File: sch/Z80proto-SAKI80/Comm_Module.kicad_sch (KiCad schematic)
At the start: 9 parts, among them J201 Conn_01x06, J202 Conn_01x06, U207 SN65HVD12HD

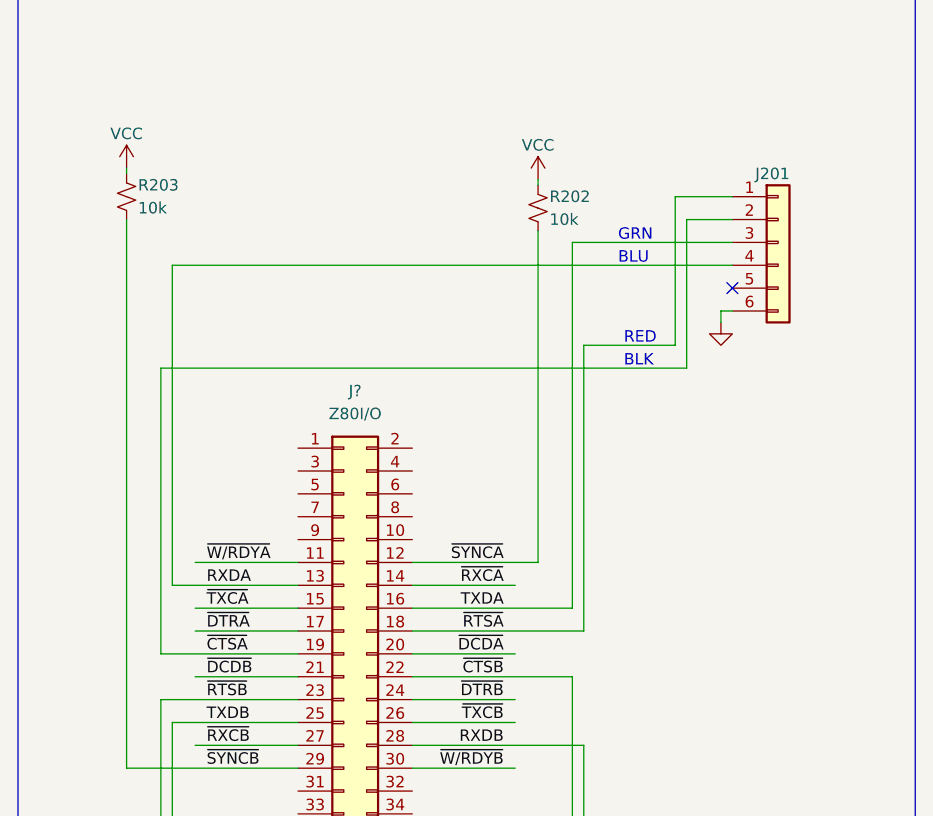
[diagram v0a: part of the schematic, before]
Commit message: add misc.
add SIO Hard flow control(but not work ...),
add WAIT implement,
add kermit implement(test).
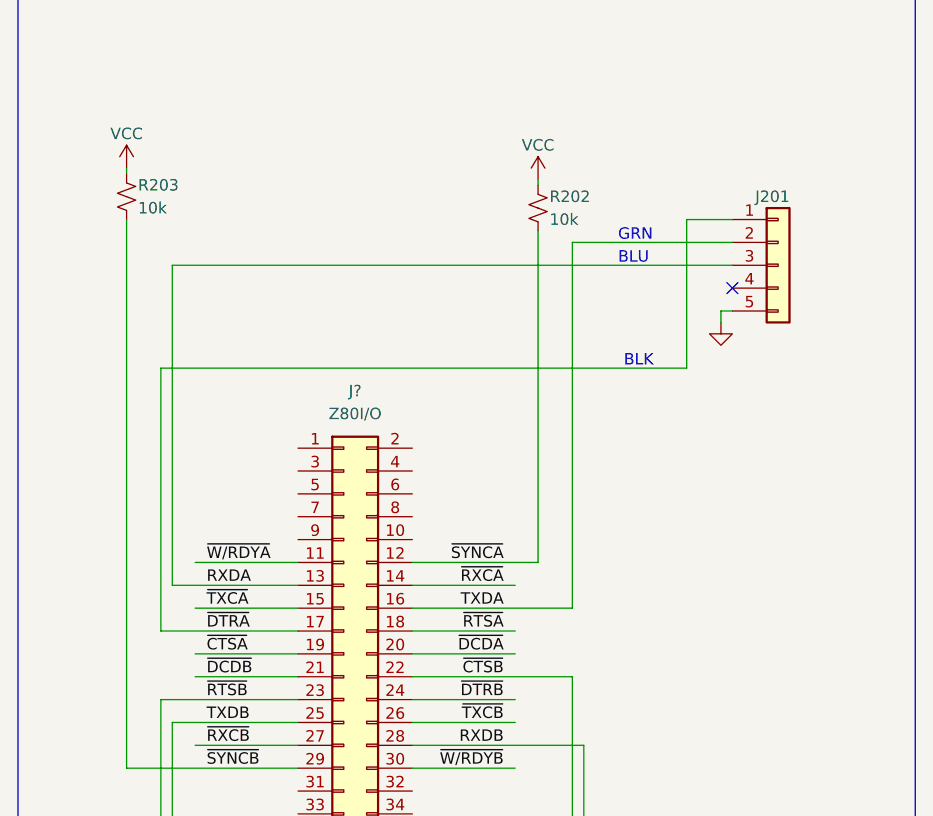
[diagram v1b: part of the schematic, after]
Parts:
- removed J201: Conn_01x06, symbol Connector_Generic:Conn_01x06
- added J201: Conn_01x05, symbol Connector_Generic:Conn_01x05
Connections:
- net GND: now also J201.5 (Pin_5)
- net RXDA: now also J201.3 (Pin_3)
- net TXDA: now also J201.2 (Pin_2)
- net ~{DTRA}: now also J201.1 (Pin_1)
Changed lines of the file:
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@@
   (no_connect (at 99.06 201.93))
   (no_connect (at 99.06 288.29))
-  (wire (pts (xy 82.55 240.03) (xy 82.55 208.28))
-    (stroke (width 0) (type default) (color 0 0 0 0))
-  )
   (wire (pts (xy 57.15 309.88) (xy 57.15 311.15))
     (stroke (width 0) (type default) (color 0 0 0 0))
@@
     (stroke (width 0) (type default) (color 0 0 0 0))
   )
-  (wire (pts (xy 35.56 242.57) (xy 50.8 242.57))
+  (wire (pts (xy 39.37 242.57) (xy 50.8 242.57))
     (stroke (width 0) (type default) (color 0 0 0 0))
   )
@@
     (stroke (width 0) (type default) (color 0 0 0 0))
   )
-  (wire (pts (xy 99.06 191.77) (xy 92.71 191.77))
-    (stroke (width 0) (type default) (color 0 0 0 0))
-  )
   (wire (pts (xy 93.98 280.67) (xy 93.98 292.1))
     (stroke (width 0) (type default) (color 0 0 0 0))
@@
     (stroke (width 0) (type default) (color 0 0 0 0))
   )
-  (wire (pts (xy 92.71 208.28) (xy 82.55 208.28))
-    (stroke (width 0) (type default) (color 0 0 0 0))
-  )
   (wire (pts (xy 36.83 250.19) (xy 50.8 250.19))
     (stroke (width 0) (type default) (color 0 0 0 0))
@@
     (stroke (width 0) (type default) (color 0 0 0 0))
   )
-  (wire (pts (xy 39.37 240.03) (xy 50.8 240.03))
+  (wire (pts (xy 35.56 240.03) (xy 50.8 240.03))
     (stroke (width 0) (type default) (color 0 0 0 0))
   )
@@
     (stroke (width 0) (type default) (color 0 0 0 0))
   )
+  (wire (pts (xy 63.5 240.03) (xy 74.93 240.03))
+    (stroke (width 0) (type default) (color 0 0 0 0))
+  )
   (wire (pts (xy 63.5 250.19) (xy 74.93 250.19))
     (stroke (width 0) (type default) (color 0 0 0 0))
   )
-  (wire (pts (xy 92.71 191.77) (xy 92.71 208.28))
-    (stroke (width 0) (type default) (color 0 0 0 0))
-  )
   (wire (pts (xy 31.75 255.27) (xy 50.8 255.27))
     (stroke (width 0) (type default) (color 0 0 0 0))
@@
     (stroke (width 0) (type default) (color 0 0 0 0))
   )
+  (wire (pts (xy 35.56 240.03) (xy 35.56 210.82))
+    (stroke (width 0) (type default) (color 0 0 0 0))
+  )
   (wire (pts (xy 82.55 285.75) (xy 82.55 318.77))
     (stroke (width 0) (type default) (color 0 0 0 0))
@@
     (stroke (width 0) (type default) (color 0 0 0 0))
   )
-  (wire (pts (xy 35.56 242.57) (xy 35.56 210.82))
-    (stroke (width 0) (type default) (color 0 0 0 0))
-  )
   (wire (pts (xy 85.09 342.9) (xy 97.79 342.9))
     (stroke (width 0) (type default) (color 0 0 0 0))
@@
     (stroke (width 0) (type default) (color 0 0 0 0))
   )
-  (wire (pts (xy 63.5 240.03) (xy 82.55 240.03))
-    (stroke (width 0) (type default) (color 0 0 0 0))
-  )
   (wire (pts (xy 36.83 199.39) (xy 36.83 234.95))
     (stroke (width 0) (type default) (color 0 0 0 0))
@@
   )
   (text "BLK" (at 87.63 292.1 0)
-    (effects (font (size 1.27 1.27)) (justify left bottom))
-  )
-  (text "RED" (at 86.995 208.28 0)
     (effects (font (size 1.27 1.27)) (justify left bottom))
   )
@@
     (pin "1")
     (pin "2")
-  )
-  (symbol (lib_id "Connector_Generic:Conn_01x06") (at 104.14 196.85 0) (unit 1)
-    (in_bom yes) (on_board yes)
-    (property "Reference" "J201" (id 0) (at 101.6 189.23 0)
-      (effects (font (size 1.27 1.27)) (justify left))
-    )
-    (property "Value" "Conn_01x06" (id 1) (at 102.87 207.01 0)
-      (effects (font (size 1.27 1.27)) (justify left) hide)
-    )
-    (property "Footprint" "" (id 2) (at 104.14 196.85 0)
-      (effects (font (size 1.27 1.27)) hide)
-    )
-    (property "Datasheet" "~" (id 3) (at 104.14 196.85 0)
-      (effects (font (size 1.27 1.27)) hide)
-    )
-    (pin "1")
-    (pin "2")
-    (pin "3")
-    (pin "4")
-    (pin "5")
-    (pin "6")
   )
   (symbol (lib_id "power:GND") (at 97.79 205.74 0) (unit 1)
@@
     (pin "1")
   )
+  (symbol (lib_id "Connector_Generic:Conn_01x05") (at 104.14 199.39 0) (unit 1)
+    (in_bom yes) (on_board yes)
+    (property "Reference" "J201" (id 0) (at 101.6 191.77 0)
+      (effects (font (size 1.27 1.27)) (justify left))
+    )
+    (property "Value" "Conn_01x05" (id 1) (at 106.68 200.6599 0)
+      (effects (font (size 1.27 1.27)) (justify left) hide)
+    )
+    (property "Footprint" "" (id 2) (at 104.14 199.39 0)
+      (effects (font (size 1.27 1.27)) hide)
+    )
+    (property "Datasheet" "~" (id 3) (at 104.14 199.39 0)
+      (effects (font (size 1.27 1.27)) hide)
+    )
+    (pin "1")
+    (pin "2")
+    (pin "3")
+    (pin "4")
+    (pin "5")
+  )
   (sheet (at 34.29 367.665) (size 54.61 27.94) (fields_autoplaced)

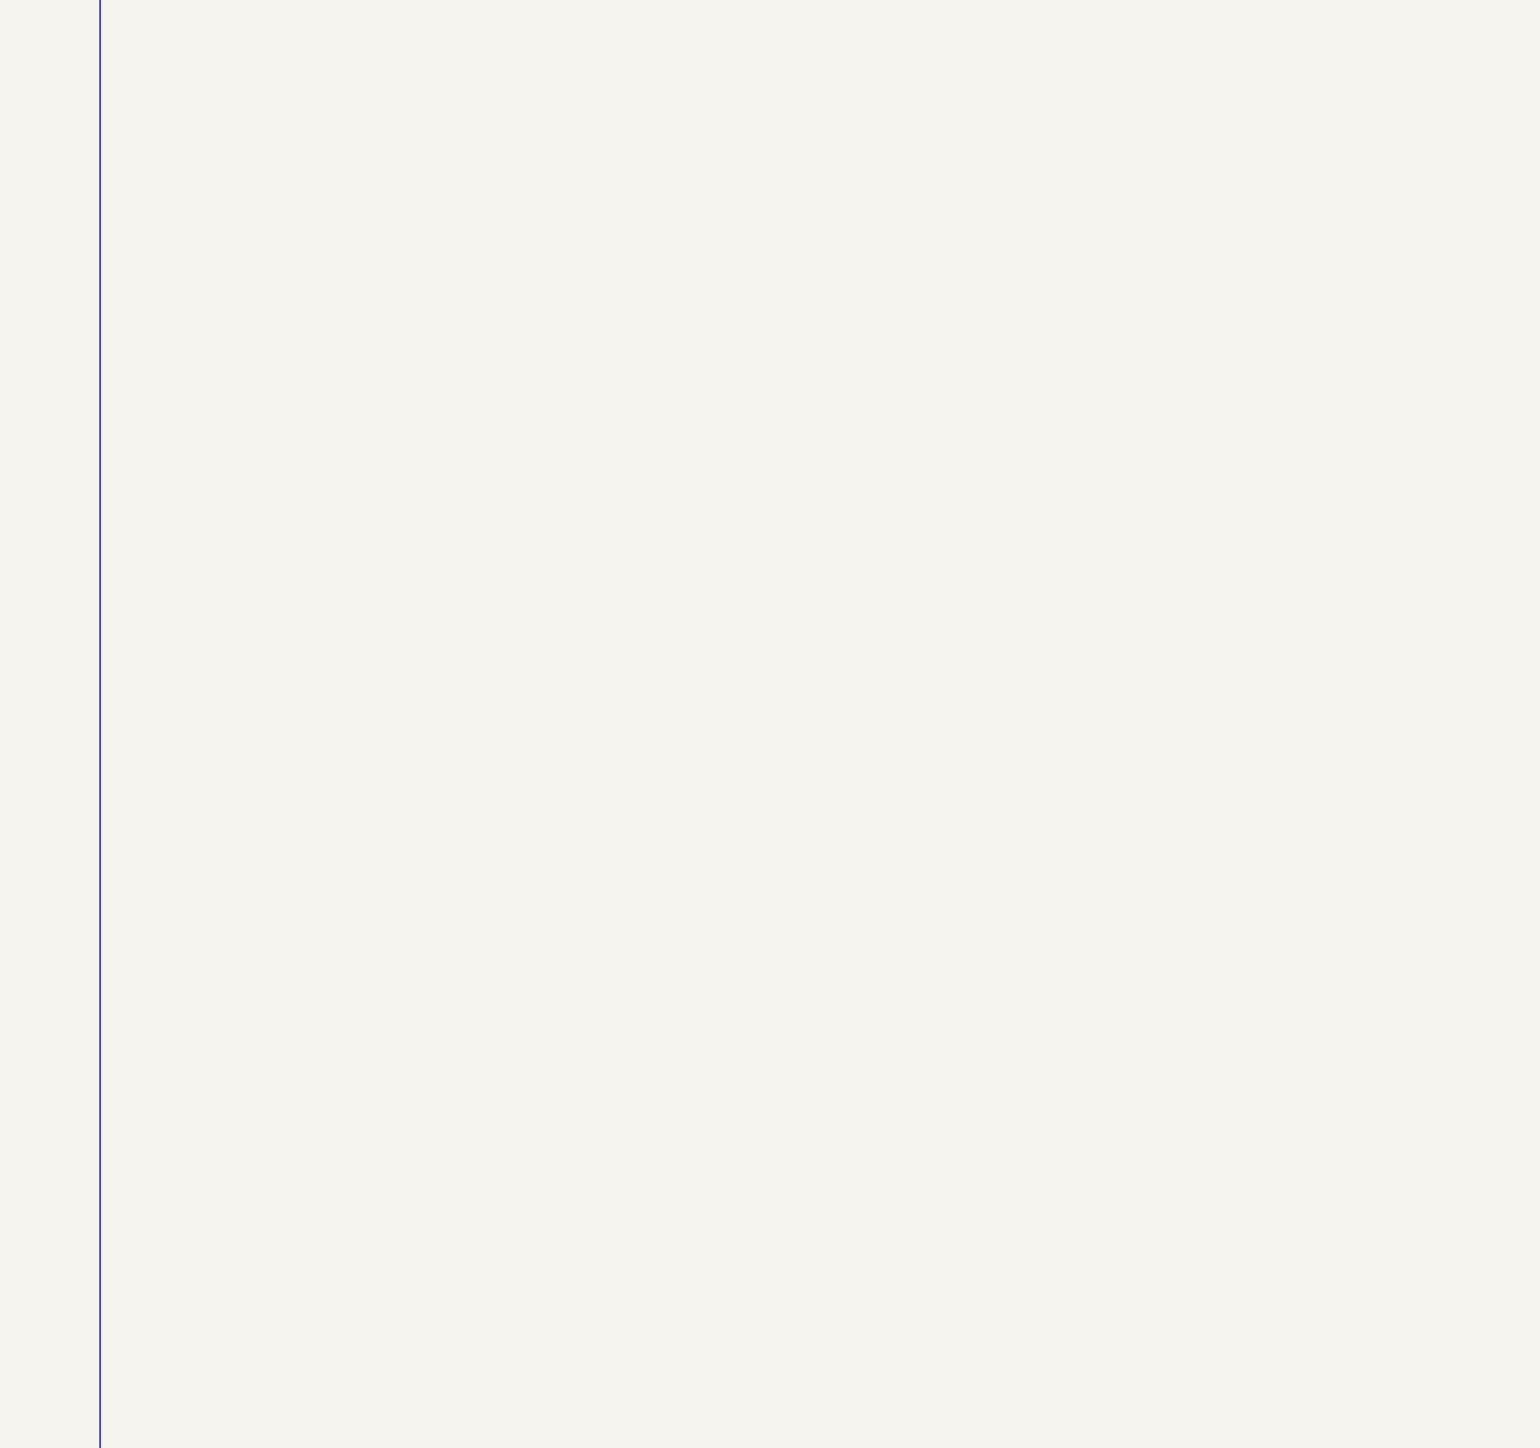
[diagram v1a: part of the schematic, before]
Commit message: EXPERIMENTAL : add reset* for FT245R
add reset line ...
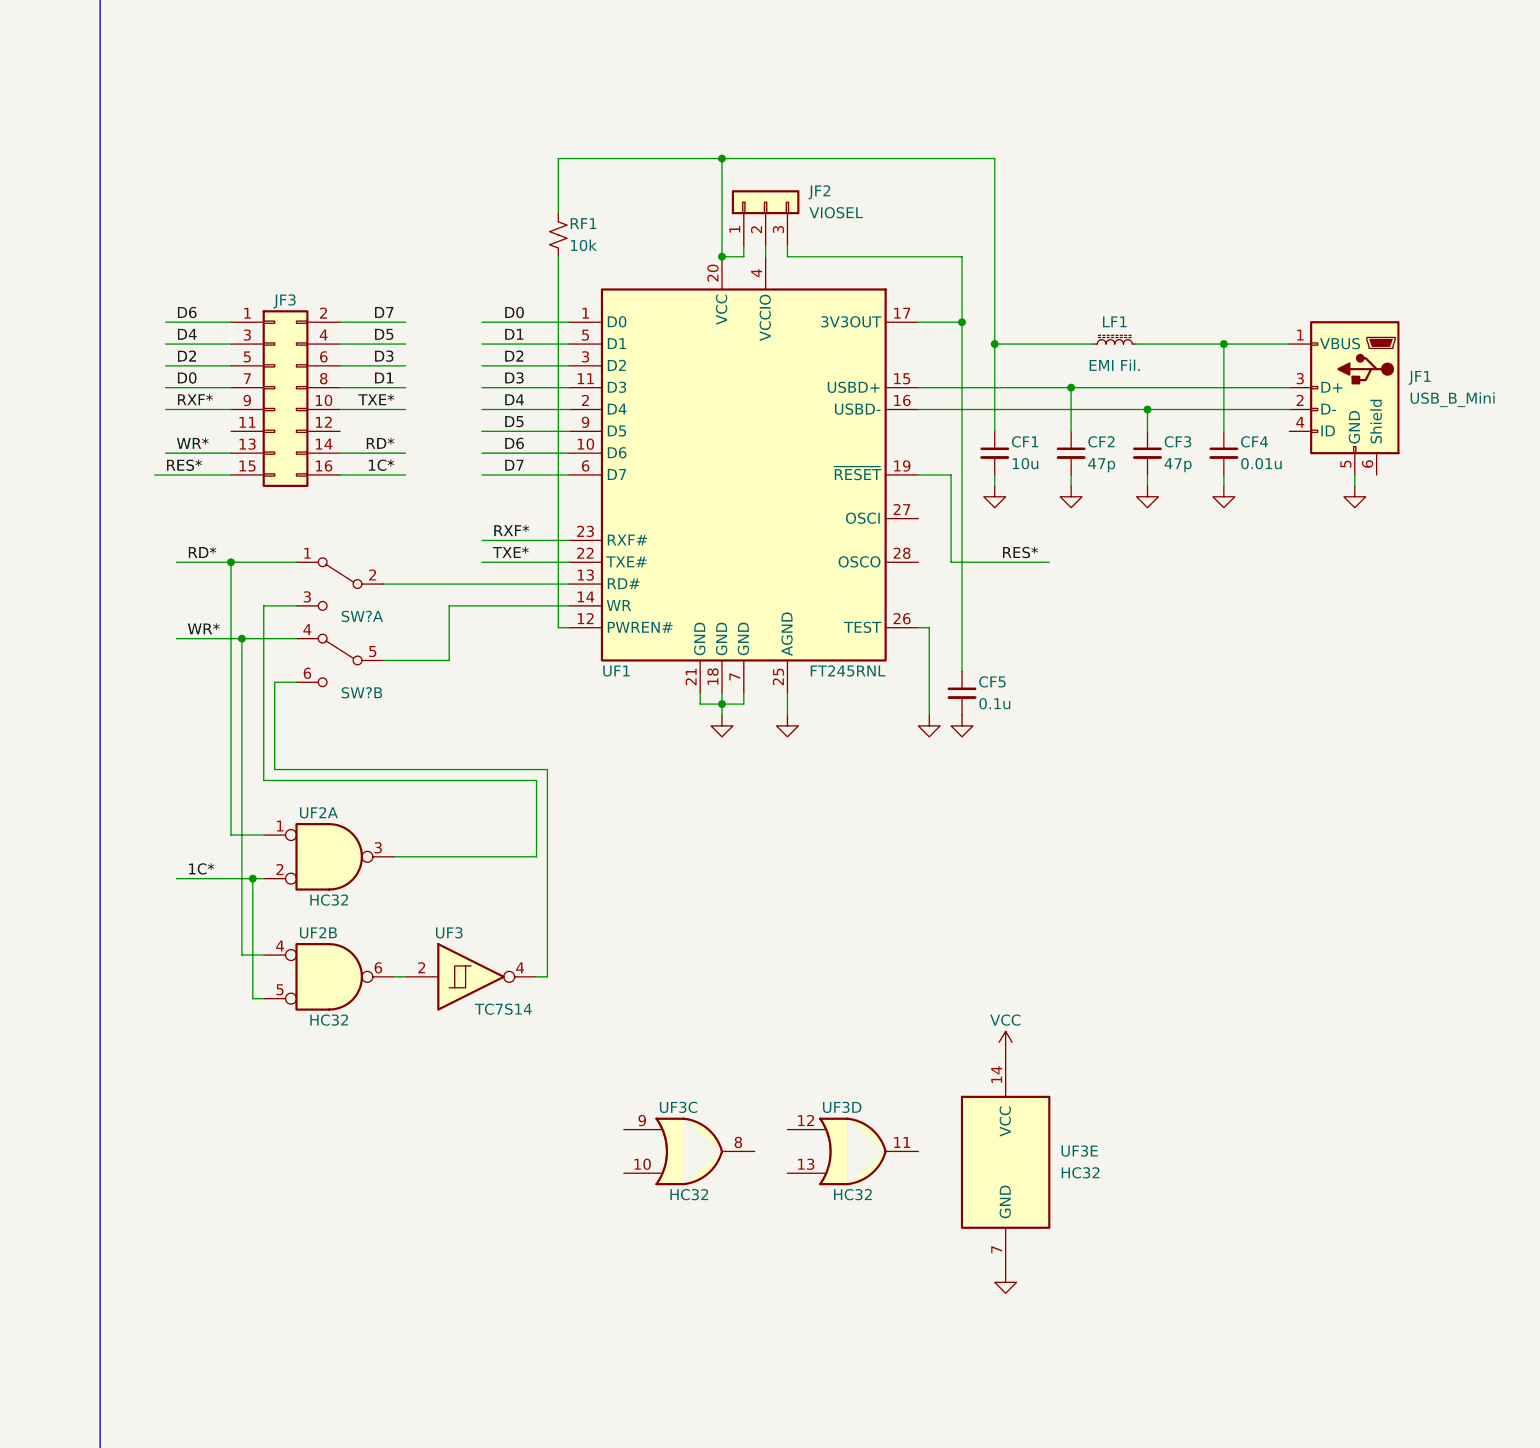
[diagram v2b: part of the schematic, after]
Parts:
- added CF1: 10u, symbol Device:C_Small
- added CF2, CF3: 47p, symbol Device:C_Small
- added CF4: 0.01u, symbol Device:C_Small
- added CF5: 0.1u, symbol Device:C_Small
- added JF1: USB_B_Mini, symbol Connector:USB_B_Mini
- added JF2: VIOSEL, symbol Connector_Generic:Conn_01x03
- added JF3: Conn_02x08_Odd_Even, symbol Connector_Generic:Conn_02x08_Odd_Even
- added LF1: EMI Fil., symbol Device:L_Ferrite_Small
- added RF1: 10k, symbol Device:R_Small_US
- added SW? (x2): SW_DPDT_x2, symbol Switch:SW_DPDT_x2
- added UF1: FT245RNL, symbol FT245RNL:FT245RNL
- added UF2: HC32, symbol 74xx:74LS32
- added UF3: TC7S14, symbol Toshiba_Sp:TC7S14
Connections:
- net GND: now also CF1.2, CF2.2, CF3.2, CF4.2, CF5.2, JF1.5 (GND), UF1.18 (GND), UF1.21 (GND), UF1.25 (AGND), UF1.26 (TEST), UF1.7 (GND), UF3.7 (GND)
- net VCC: now also UF3.14 (VCC)
- new net: CF5.1, JF2.3 (Pin_3), UF1.17 (3V3OUT)
- new net: CF4.1, JF1.1 (VBUS), LF1.2
- new net: CF3.1, JF1.2 (D-), UF1.16 (USBD-)
- new net: CF2.1, JF1.3 (D+), UF1.15 (USBD+)
- new net: CF1.1, JF2.1 (Pin_1), LF1.1, RF1.1, UF1.20 (VCC)
- new net: RF1.2, UF1.12 (PWREN#)
- new net: UF2.6, UF3.2
- new net: SW?.6 (C), UF3.4
- new net: SW?.2 (B), UF1.13 (RD#)
- new net: SW?.5 (B), UF1.14 (WR)
- new net: JF2.2 (Pin_2), UF1.4 (VCCIO)
- new net: SW?.3 (C), UF2.3
- new net 1C*: JF3.16 (Pin_16), UF2.2, UF2.5
- new net D0: JF3.7 (Pin_7), UF1.1 (D0)
- new net D1: JF3.8 (Pin_8), UF1.5 (D1)
- new net D2: JF3.5 (Pin_5), UF1.3 (D2)
- new net D3: JF3.6 (Pin_6), UF1.11 (D3)
- new net D4: JF3.3 (Pin_3), UF1.2 (D4)
- new net D5: JF3.4 (Pin_4), UF1.9 (D5)
- new net D6: JF3.1 (Pin_1), UF1.10 (D6)
- new net D7: JF3.2 (Pin_2), UF1.6 (D7)
- new net RD*: JF3.14 (Pin_14), SW?.1 (A), UF2.1
- new net RES*: JF3.15 (Pin_15), UF1.19 (~{RESET})
- new net RXF*: JF3.9 (Pin_9), UF1.23 (RXF#)
- new net TXE*: JF3.10 (Pin_10), UF1.22 (TXE#)
- new net WR*: JF3.13 (Pin_13), SW?.4 (A), UF2.4
